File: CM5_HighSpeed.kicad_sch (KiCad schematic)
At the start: 11 parts, among them J5 Conn_01x22_Female, J6 THD-02-R, U6 AP22653W6

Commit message: end of jan 11th
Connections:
- no-connect marks 26 -> 47
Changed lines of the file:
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@@
+	)
+	(no_connect
+		(at 115.57 99.06)
+	)
+	(no_connect
+		(at 115.57 127)
 	)
 	(no_connect
@@
 	)
 	(no_connect
+		(at 115.57 86.36)
+	)
+	(no_connect
+		(at 115.57 142.24)
+	)
+	(no_connect
+		(at 115.57 134.62)
+	)
+	(no_connect
 		(at 21.59 99.06)
 	)
 	(no_connect
+		(at 115.57 149.86)
+	)
+	(no_connect
+		(at 115.57 96.52)
+	)
+	(no_connect
 		(at 21.59 142.24)
 	)
 	(no_connect
+		(at 115.57 104.14)
+	)
+	(no_connect
+		(at 115.57 114.3)
+	)
+	(no_connect
+		(at 115.57 129.54)
+	)
+	(no_connect
 		(at 21.59 111.76)
 	)
 	(no_connect
+		(at 115.57 119.38)
+	)
+	(no_connect
+		(at 115.57 83.82)
+	)
+	(no_connect
+		(at 115.57 88.9)
+	)
+	(no_connect
 		(at 21.59 144.78)
 	)
@@
 	)
 	(no_connect
+		(at 115.57 137.16)
+	)
+	(no_connect
 		(at 21.59 121.92)
 	)
@@
 	)
 	(no_connect
+		(at 115.57 121.92)
+	)
+	(no_connect
 		(at 21.59 106.68)
 	)
 	(no_connect
+		(at 115.57 106.68)
+	)
+	(no_connect
+		(at 115.57 91.44)
+	)
+	(no_connect
 		(at 21.59 114.3)
 	)
@@
 	)
 	(no_connect
+		(at 115.57 78.74)
+	)
+	(no_connect
+		(at 115.57 81.28)
+	)
+	(no_connect
 		(at 21.59 66.04)
+	)
+	(no_connect
+		(at 115.57 144.78)
+	)
+	(no_connect
+		(at 115.57 111.76)
 	)
 	(no_connect
@@
 		(effects
 			(font
+				(size 1.27 1.27)
+			)
+			(justify right)
+		)
+	)
+	(hierarchical_label "+5v"
+		(shape input)
+		(at 24.13 175.26 180)
+		(effects
+			(font

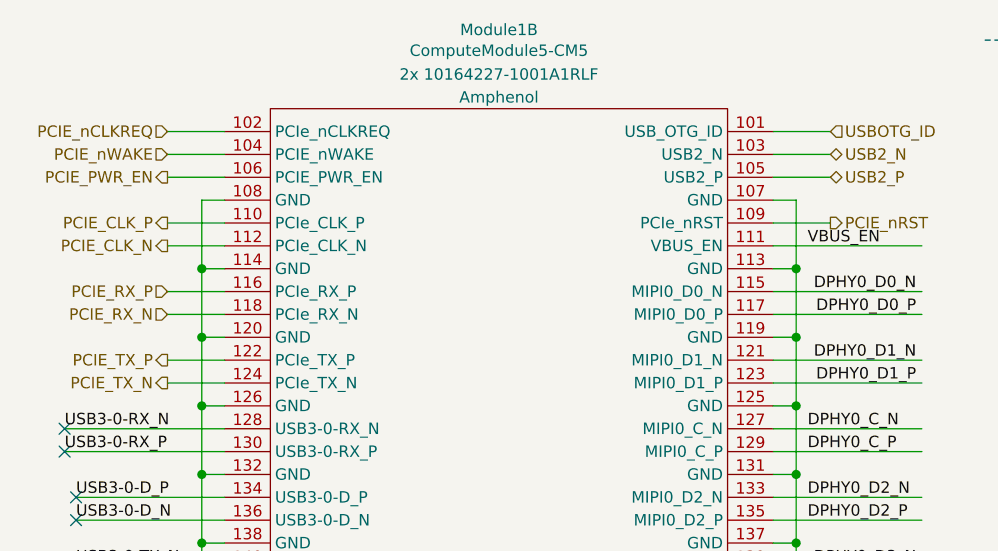
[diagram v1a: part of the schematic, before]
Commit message: Removed ERC errors and M2 connector
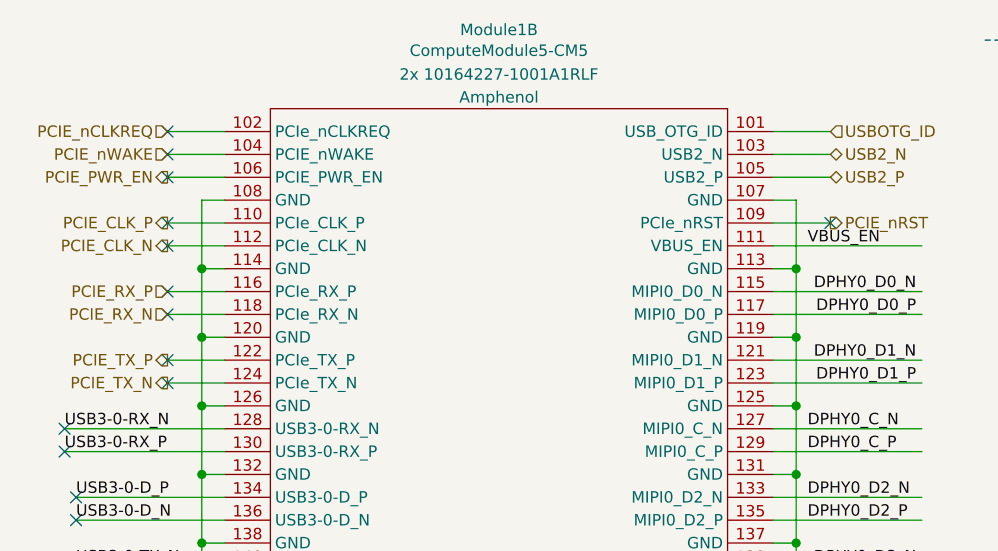
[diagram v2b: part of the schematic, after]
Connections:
- no-connect marks 47 -> 57
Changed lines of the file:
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@@
+	)
+	(no_connect
+		(at 31.75 30.48)
 	)
 	(no_connect
@@
 	)
 	(no_connect
+		(at 31.75 35.56)
+	)
+	(no_connect
 		(at 115.57 142.24)
 	)
@@
 	)
 	(no_connect
+		(at 31.75 38.1)
+	)
+	(no_connect
 		(at 115.57 149.86)
 	)
@@
 	)
 	(no_connect
+		(at 31.75 45.72)
+	)
+	(no_connect
 		(at 21.59 142.24)
+	)
+	(no_connect
+		(at 31.75 53.34)
 	)
 	(no_connect
@@
 	)
 	(no_connect
+		(at 31.75 27.94)
+	)
+	(no_connect
 		(at 115.57 119.38)
 	)
@@
 	(no_connect
 		(at 115.57 88.9)
+	)
+	(no_connect
+		(at 31.75 50.8)
+	)
+	(no_connect
+		(at 31.75 25.4)
 	)
 	(no_connect
@@
 	)
 	(no_connect
+		(at 31.75 43.18)
+	)
+	(no_connect
 		(at 21.59 91.44)
 	)
@@
 	)
 	(no_connect
+		(at 105.41 35.56)
+	)
+	(no_connect
